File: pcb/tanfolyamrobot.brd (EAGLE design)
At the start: 81.3 x 58.7 mm, 81 parts, among them IC1 STM32F10XRXT6, IC2 7805, IC4 FT232RL, IC5 LD117AS33TR, M1 DRV8833, Q1 AO4407A, Q2 BSS123, Q3 BSS123, Q4 BSS123, X1 CSTCE08M, X2 PWR

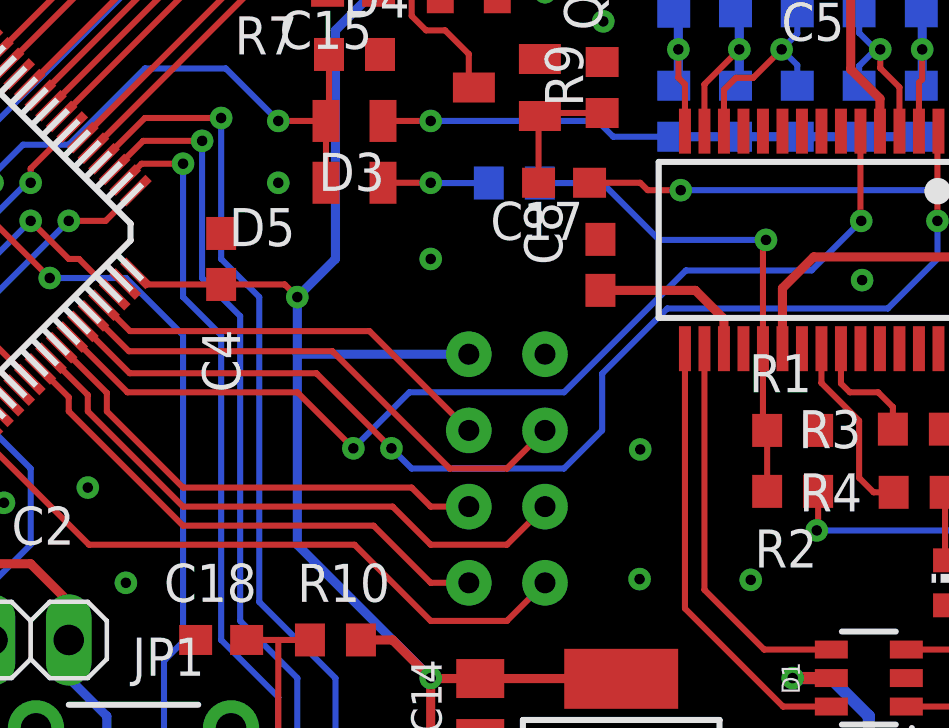
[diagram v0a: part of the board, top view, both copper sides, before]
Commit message: added usb power detection (#1)
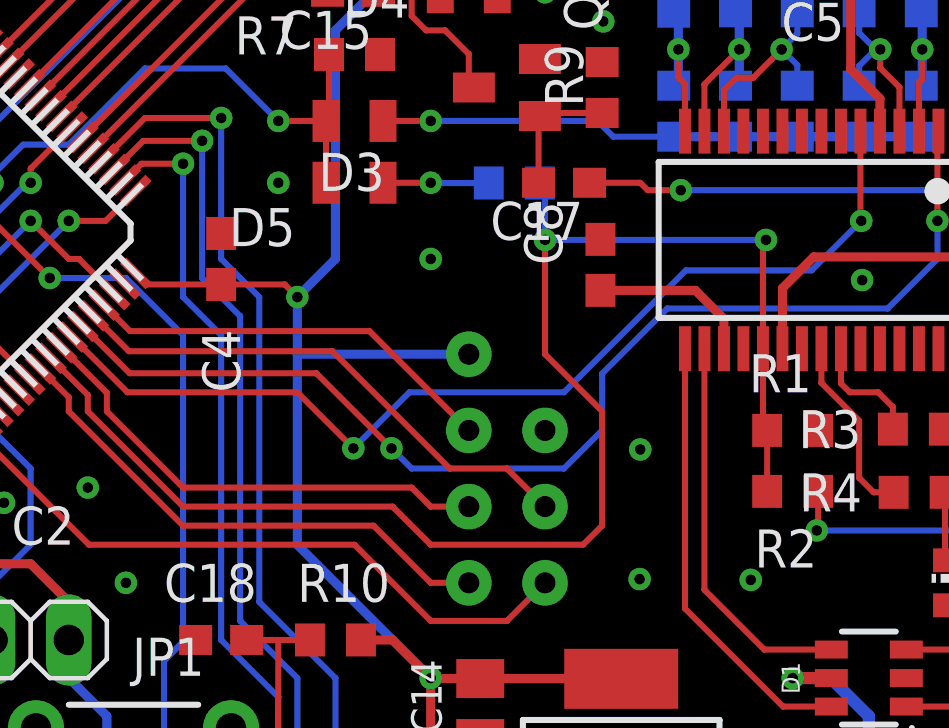
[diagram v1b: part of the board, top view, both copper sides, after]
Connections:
- removed net FTDI_RSTN: IC4.19, R1.2, R2.1, R28.1
- removed net PC9: IC1.40
- new net USB_PWR_DET: IC1.40, IC4.19, R1.2, R2.1, R28.1
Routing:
- net USB_PWR_DET: track 0.00 -> 49.7 mm, vias 0 -> 2
- net PC9: track 19.9 -> 0.00 mm, vias 1 -> 0
- net FTDI_RSTN: track 16.8 -> 0.00 mm, vias 1 -> 0
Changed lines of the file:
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@@
 <grid distance="25" unitdist="mil" unit="mil" style="dots" multiple="1" display="yes" altdistance="6.125" altunitdist="mil" altunit="mil"/>
 <layers>
-<layer number="1" name="Top" color="4" fill="1" visible="no" active="yes"/>
+<layer number="1" name="Top" color="4" fill="1" visible="yes" active="yes"/>
 <layer number="2" name="Route2" color="16" fill="1" visible="no" active="no"/>
 <layer number="3" name="Route3" color="17" fill="1" visible="no" active="no"/>
@@
 <layer number="19" name="Unrouted" color="6" fill="1" visible="yes" active="yes"/>
 <layer number="20" name="Dimension" color="24" fill="1" visible="yes" active="yes"/>
-<layer number="21" name="tPlace" color="7" fill="1" visible="no" active="yes"/>
+<layer number="21" name="tPlace" color="7" fill="1" visible="yes" active="yes"/>
 <layer number="22" name="bPlace" color="7" fill="1" visible="yes" active="yes"/>
-<layer number="23" name="tOrigins" color="13" fill="1" visible="no" active="yes"/>
+<layer number="23" name="tOrigins" color="13" fill="1" visible="yes" active="yes"/>
 <layer number="24" name="bOrigins" color="13" fill="1" visible="yes" active="yes"/>
 <layer number="25" name="tNames" color="7" fill="1" visible="no" active="yes"/>
@@
 <layer number="37" name="tTest" color="7" fill="1" visible="no" active="yes"/>
 <layer number="38" name="bTest" color="7" fill="1" visible="no" active="yes"/>
-<layer number="39" name="tKeepout" color="4" fill="11" visible="no" active="yes"/>
-<layer number="40" name="bKeepout" color="1" fill="11" visible="no" active="yes"/>
-<layer number="41" name="tRestrict" color="4" fill="10" visible="no" active="yes"/>
-<layer number="42" name="bRestrict" color="1" fill="10" visible="no" active="yes"/>
+<layer number="39" name="tKeepout" color="4" fill="11" visible="yes" active="yes"/>
+<layer number="40" name="bKeepout" color="1" fill="11" visible="yes" active="yes"/>
+<layer number="41" name="tRestrict" color="4" fill="10" visible="yes" active="yes"/>
+<layer number="42" name="bRestrict" color="1" fill="10" visible="yes" active="yes"/>
 <layer number="43" name="vRestrict" color="2" fill="10" visible="no" active="yes"/>
 <layer number="44" name="Drills" color="7" fill="1" visible="no" active="yes"/>
@@
 <layer number="49" name="Reference" color="7" fill="1" visible="no" active="yes"/>
 <layer number="50" name="dxf" color="7" fill="1" visible="no" active="no"/>
-<layer number="51" name="tDocu" color="7" fill="1" visible="no" active="yes"/>
+<layer number="51" name="tDocu" color="7" fill="1" visible="yes" active="yes"/>
 <layer number="52" name="bDocu" color="7" fill="1" visible="yes" active="yes"/>
 <layer number="53" name="tGND_GNDA" color="7" fill="9" visible="no" active="no"/>
@@
 </layers>
 <board>
-<fusionsync huburn="a.cGVyc29uYWw6dWUyZDE5ZTY1" projecturn="a.cGVyc29uYWw6dWUyZDE5ZTY1IzIwMTgxMDI1MTU2NjUyNjAx" f3durn="urn:adsk.wipprod:dm.lineage:5JW7hhN6Qia-GW_hkwh2aQ" pcbguid="3c9f62af-45f0-4480-b892-c83412483946" lastpulledtime="" lastsyncedchangeguid="42398600-4bea-8ae5-8252-3c352434bef0"/>
+<fusionsync huburn="a.cGVyc29uYWw6dWUyZDE5ZTY1" projecturn="a.cGVyc29uYWw6dWUyZDE5ZTY1IzIwMTgxMDI1MTU2NjUyNjAx" f3durn="urn:adsk.wipprod:dm.lineage:5JW7hhN6Qia-GW_hkwh2aQ" pcbguid="3c9f62af-45f0-4480-b892-c83412483946" lastpulledtime="" lastsyncedchangeguid="42398600-4bea-8ae5-8252-3c352434bef0" latestrevisionid="" lastsyncedrevisionid="" lastboardhashguid="" lastpushedtime="" linktopcb3d="false"/>
 <plain>
 <wire x1="0" y1="0" x2="81.26" y2="0" width="0" layer="20"/>
@@
 <via x="27.308175" y="47.98695" extent="1-16" drill="0.35"/>
 <via x="6.985" y="24.765" extent="1-16" drill="0.35"/>
-<via x="52.705" y="29.21" extent="1-16" drill="0.7" diameter="1.524"/>
+<via x="52.705" y="26.67" extent="1-16" drill="0.7" diameter="1.524"/>
 <via x="63.5" y="50.165" extent="1-16" drill="0.35"/>
 <via x="48.895" y="54.61" extent="1-16" drill="0.35"/>
@@
 <via x="71.214425" y="52.77885" extent="1-16" drill="0.35"/>
 </signal>
-<signal name="FTDI_RSTN">
+<signal name="USB_PWR_DET">
 <contactref element="R2" pad="1"/>
 <contactref element="IC4" pad="19"/>
@@
 <wire x1="59.97" y1="32.919" x2="60.071" y2="33.02" width="0.2032" layer="1"/>
 <contactref element="R28" pad="1"/>
-<wire x1="60.071" y1="33.02" x2="56.515" y2="33.02" width="0.2032" layer="16"/>
-<wire x1="54.619525" y1="34.915475" x2="52.53265" y2="34.915475" width="0.2032" layer="16"/>
-<wire x1="56.515" y1="33.02" x2="54.619525" y2="34.915475" width="0.2032" layer="16"/>
 <wire x1="59.97" y1="29.395" x2="59.97" y2="26.81" width="0.2032" layer="1"/>
 <wire x1="59.97" y1="26.81" x2="60.11" y2="26.67" width="0.2032" layer="1"/>
 <wire x1="60.11" y1="26.67" x2="60.11" y2="24.638" width="0.2032" layer="1"/>
+<contactref element="IC1" pad="40"/>
+<wire x1="36.23873125" y1="29.0757375" x2="37.465" y2="27.84946875" width="0.2032" layer="1"/>
+<wire x1="37.465" y1="27.84946875" x2="37.465" y2="27.305" width="0.2032" layer="1"/>
+<wire x1="47.625" y1="24.13" x2="48.895" y2="22.86" width="0.2032" layer="1"/>
+<wire x1="48.895" y1="22.86" x2="53.975" y2="22.86" width="0.2032" layer="1"/>
+<wire x1="53.975" y1="22.86" x2="54.61" y2="23.495" width="0.2032" layer="1"/>
+<wire x1="37.465" y1="27.305" x2="40.64" y2="24.13" width="0.2032" layer="1"/>
+<wire x1="40.64" y1="24.13" x2="47.625" y2="24.13" width="0.2032" layer="1"/>
+<wire x1="54.61" y1="23.495" x2="54.61" y2="27.305" width="0.2032" layer="1"/>
+<wire x1="54.61" y1="27.305" x2="52.705" y2="29.21" width="0.2032" layer="1"/>
+<wire x1="52.705" y1="29.21" x2="52.705" y2="33.02" width="0.2032" layer="1"/>
+<via x="52.705" y="33.02" extent="1-16" drill="0.35"/>
+<wire x1="60.071" y1="33.02" x2="52.705" y2="33.02" width="0.2032" layer="16"/>
+<wire x1="52.705" y1="33.02" x2="52.705" y2="34.743125" width="0.2032" layer="16"/>
+<wire x1="52.705" y1="34.743125" x2="52.53265" y2="34.915475" width="0.2032" layer="16"/>
 </signal>
 <signal name="FTDI_TXLEDN_R">
@@
 <contactref element="IC1" pad="44"/>
 <wire x1="37.65294375" y1="30.489953125" x2="38.83395" y2="29.308946875" width="0.2032" layer="1"/>
-<via x="52.705" y="26.67" extent="1-16" drill="0.7" diameter="1.524"/>
+<via x="52.705" y="24.13" extent="1-16" drill="0.7" diameter="1.524"/>
 <wire x1="38.83395" y1="29.308946875" x2="45.621053125" y2="29.308946875" width="0.2032" layer="1"/>
-<wire x1="51.435" y1="25.4" x2="52.705" y2="26.67" width="0.2032" layer="1"/>
+<wire x1="51.435" y1="25.4" x2="52.705" y2="24.13" width="0.2032" layer="1"/>
 <wire x1="45.621053125" y1="29.308946875" x2="49.53" y2="25.4" width="0.2032" layer="1"/>
 <wire x1="49.53" y1="25.4" x2="51.435" y2="25.4" width="0.2032" layer="1"/>
@@
 <wire x1="46.99" y1="23.495" x2="48.895" y2="21.59" width="0.2032" layer="1"/>
 </signal>
-<signal name="PC9">
-<contactref element="IC1" pad="40"/>
-<via x="52.705" y="24.13" extent="1-16" drill="0.7" diameter="1.524"/>
-<wire x1="52.705" y1="24.13" x2="51.435" y2="22.86" width="0.2032" layer="1"/>
-<wire x1="37.465" y1="27.305" x2="40.64" y2="24.13" width="0.2032" layer="1"/>
-<wire x1="51.435" y1="22.86" x2="48.895" y2="22.86" width="0.2032" layer="1"/>
-<wire x1="48.895" y1="22.86" x2="47.625" y2="24.13" width="0.2032" layer="1"/>
-<wire x1="47.625" y1="24.13" x2="40.64" y2="24.13" width="0.2032" layer="1"/>
-<wire x1="36.23873125" y1="29.0757375" x2="37.465" y2="27.84946875" width="0.2032" layer="1"/>
-<wire x1="37.465" y1="27.84946875" x2="37.465" y2="27.305" width="0.2032" layer="1"/>
-</signal>
 <signal name="PA4">

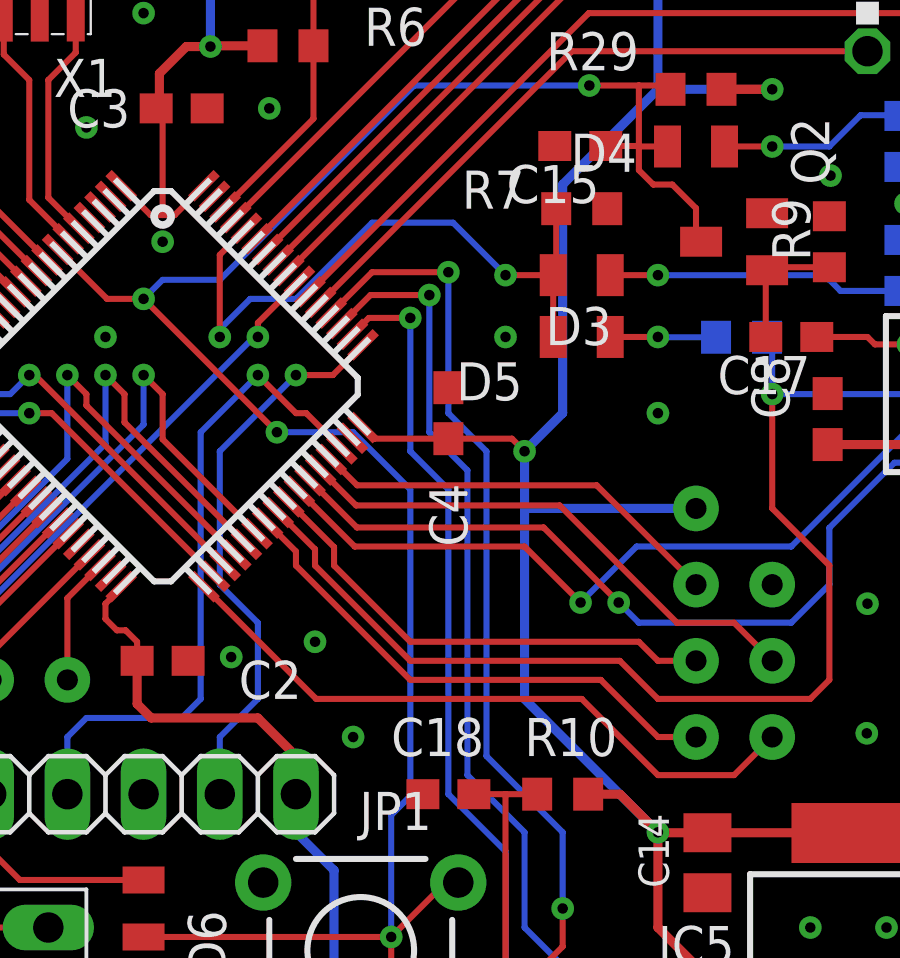
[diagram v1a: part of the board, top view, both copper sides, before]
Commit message: made traces of unused pins nicer (#1)
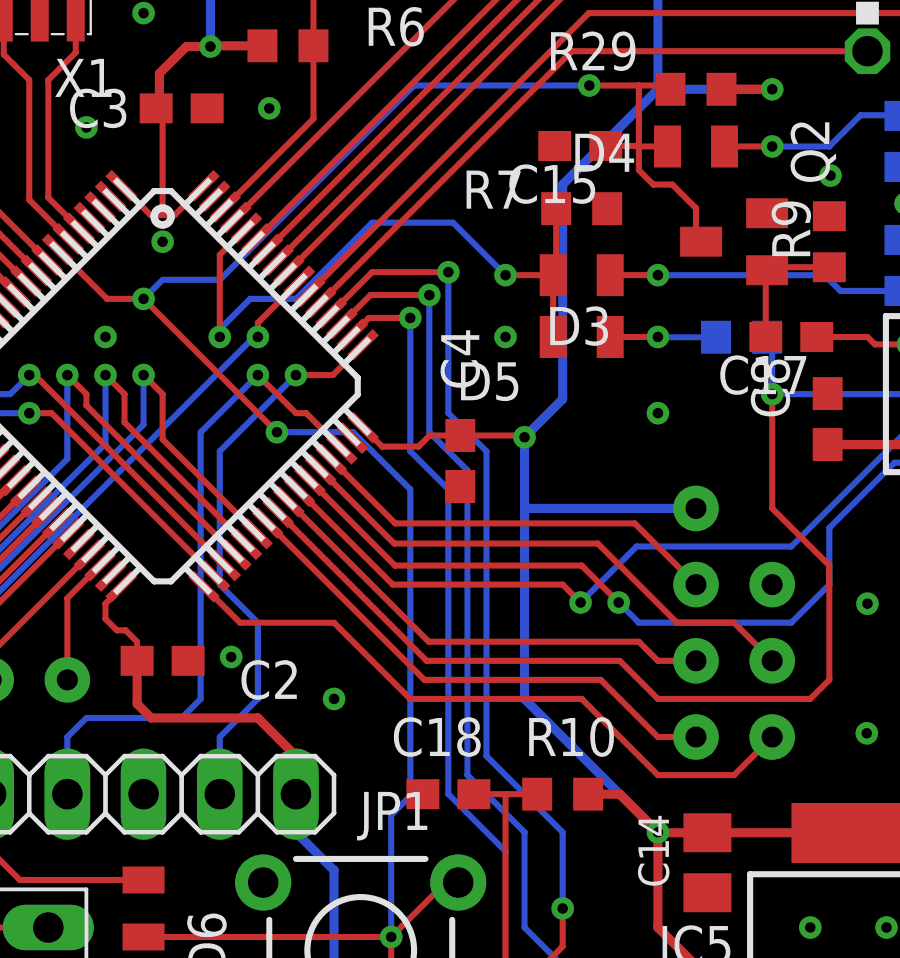
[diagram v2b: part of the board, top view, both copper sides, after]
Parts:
- moved C4 1.64 mm to (42.3, 30.8), turned to 270 degrees
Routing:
- net GND: vias 55 -> 54

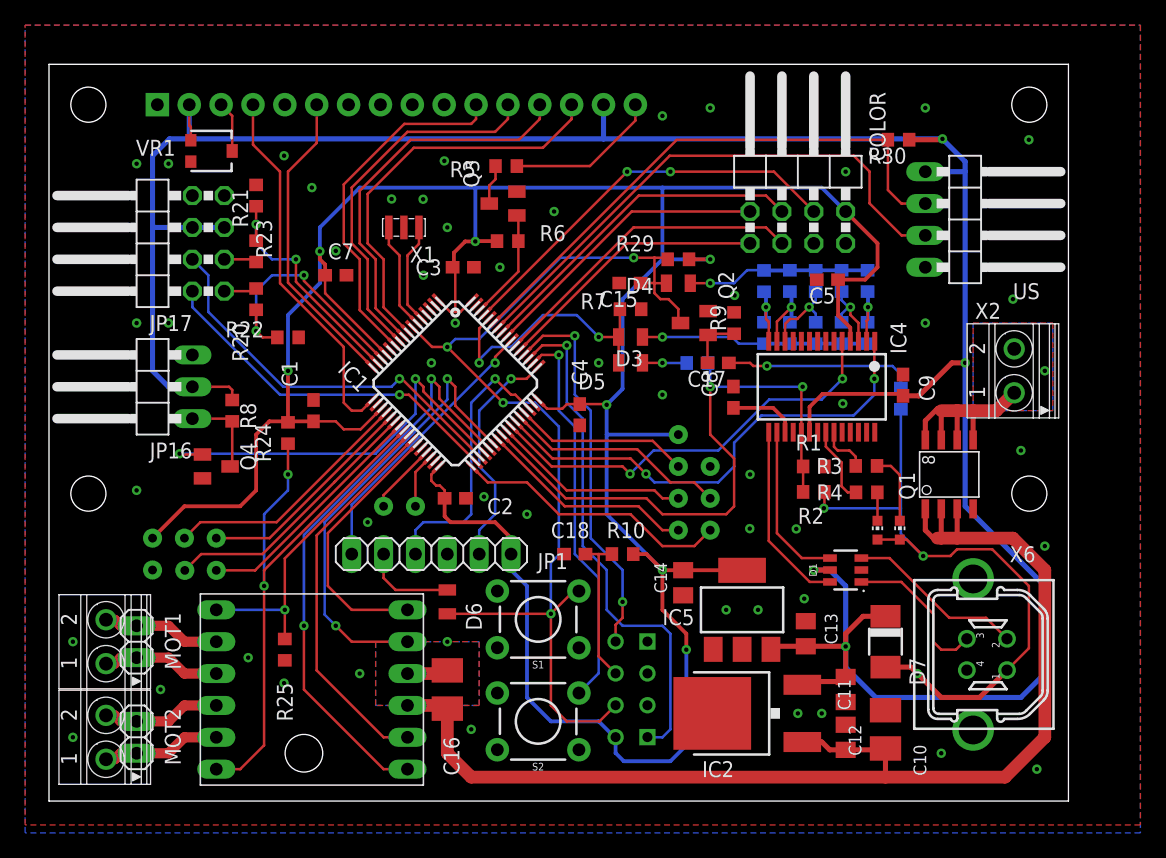
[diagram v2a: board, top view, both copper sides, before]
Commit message: fixed encoder stm32 connections (#1)
also had to move lcd pins
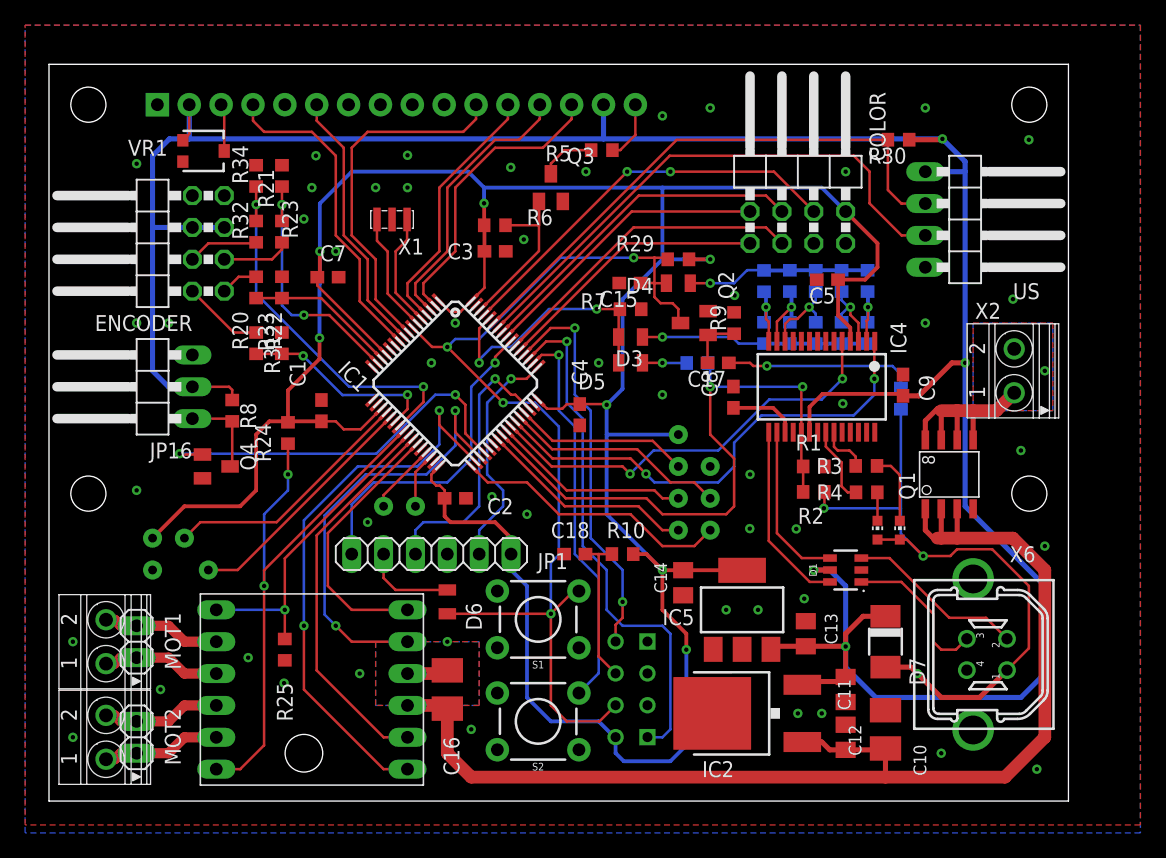
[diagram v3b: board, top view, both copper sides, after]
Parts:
- added R31, R32: 10K, rcl:R0603
- added R33, R34: 20K, rcl:R0603
- moved R5 7.73 mm to (44.1, 51.9)
- moved Q3 4.02 mm to (40.0, 48.9), turned to 0 degrees
- moved R22 4.01 mm to (18.6, 40.9), turned to 90 degrees
- moved C3 2.84 mm to (35.6, 43.8)
- moved R21 2.59 mm to (18.6, 45.4)
- moved R23 2.59 mm to (18.6, 49.8)
- moved R6 1.63 mm to (35.5, 45.9)
- moved X1 1.14 mm to (27.3, 46.4)
- moved R20 0.93 mm to (16.5, 40.9)
- moved C7 0.64 mm to (22.2, 41.8)
- moved VR1 0.63 mm to (12.3, 51.8)
- moved C1 0.63 mm to (21.7, 31.1)
- renumbered JP17 to ENCODER
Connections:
- removed net PA6: IC1.22
- removed net PA7: IC1.23
- new net ENC2_A_3V3: IC1.22, R31.2, R33.1
- new net ENC2_B_3V3: IC1.23, R32.2, R34.1
- new net PC3: IC1.11
- new net PC6: IC1.37
- new net PC7: IC1.38
- net ENC2_A_5V: now also R31.1; no longer IC1.34
- net ENC2_B_5V: now also R32.1; no longer IC1.35
- net GND: now also R33.2, R34.2
- net LCD_D4: now also IC1.8; no longer IC1.11
- net LCD_D5: now also IC1.4; no longer IC1.10
- net LCD_D6: now also IC1.3; no longer IC1.9
- net LCD_D7: now also IC1.2; no longer IC1.8
- net LCD_EN: now also IC1.9; no longer IC1.16
- net LCD_RST: now also IC1.10; no longer IC1.17
- net MOTOR1_IN1: now also IC1.34; no longer IC1.37
- net MOTOR2_IN1: now also IC1.35; no longer IC1.38
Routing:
- net ENC2_B_3V3: track 0.00 -> 30.3 mm, vias 0 -> 2
- net ENC2_B_5V: track 31.9 -> 5.64 mm, vias 1 -> 0
- net ENC2_A_5V: track 29.1 -> 6.45 mm, vias 1 -> 0
- net PA6: track 21.5 -> 0.00 mm, vias 1 -> 0
- net PA7: track 19.2 -> 0.00 mm, vias 1 -> 0
- net ENC2_A_3V3: track 0.00 -> 16.1 mm, vias 0 -> 2
- net LCD_D5: track 29.5 -> 20.5 mm
- net LCD_D6: track 30.8 -> 21.9 mm
- net LCD_D7: track 32.1 -> 23.4 mm
- net ENC1_A_3V3: track 20.2 -> 11.9 mm, vias 2 -> 0
- net N$6: track 12.2 -> 4.74 mm
- net LCD_BACKLIGHT: track 8.68 -> 15.0 mm
- net LCD_RST: track 29.5 -> 25.7 mm
- net SWD_SWO: track 22.5 -> 25.8 mm
- net LCD_EN: track 24.5 -> 21.2 mm
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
